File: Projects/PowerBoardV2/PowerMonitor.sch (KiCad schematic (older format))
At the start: 33 parts, among them M1 Teensy3, P19 CAN_CONN, P20 BAT_CONN, U1 ACS712, U2 MCP2562, U3 ACS712

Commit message: Trying to replace current resistors with surface mount resistors
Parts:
- R1, R10, R11, R12, R13, R14, R15, R16, R17, R18, R19, R2, R20, R3, R4, R5, R6, R7, R8, R9: footprint Resistors_ThroughHole:Resistor_Horizontal_RM7mm -> Resistors_SMD:R_0805_HandSoldering
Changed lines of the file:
@@
 F 0 "R1" V 4030 3300 50  0000 C CNN
 F 1 "2k" V 3950 3300 50  0000 C CNN
-F 2 "Resistors_ThroughHole:Resistor_Horizontal_RM7mm" V 3880 3300 50  0001 C CNN
+F 2 "Resistors_SMD:R_0805_HandSoldering" V 3880 3300 50  0001 C CNN
 F 3 "" H 3950 3300 50  0000 C CNN
 	1    3950 3300
@@
 F 0 "R2" V 4280 3500 50  0000 C CNN
 F 1 "10k" V 4200 3500 50  0000 C CNN
-F 2 "Resistors_ThroughHole:Resistor_Horizontal_RM7mm" V 4130 3500 50  0001 C CNN
+F 2 "Resistors_SMD:R_0805_HandSoldering" V 4130 3500 50  0001 C CNN
 F 3 "" H 4200 3500 50  0000 C CNN
 	1    4200 3500
@@
 F 0 "R5" V 6980 3650 50  0000 C CNN
 F 1 "886k" V 6900 3650 50  0000 C CNN
-F 2 "Resistors_ThroughHole:Resistor_Horizontal_RM7mm" V 6830 3650 50  0001 C CNN
+F 2 "Resistors_SMD:R_0805_HandSoldering" V 6830 3650 50  0001 C CNN
 F 3 "" H 6900 3650 50  0000 C CNN
 	1    6900 3650
@@
 F 0 "R6" V 6980 3850 50  0000 C CNN
 F 1 "870k" V 6900 3850 50  0000 C CNN
-F 2 "Resistors_ThroughHole:Resistor_Horizontal_RM7mm" V 6830 3850 50  0001 C CNN
+F 2 "Resistors_SMD:R_0805_HandSoldering" V 6830 3850 50  0001 C CNN
 F 3 "" H 6900 3850 50  0000 C CNN
 	1    6900 3850
@@
 F 0 "R7" V 6980 4050 50  0000 C CNN
 F 1 "848k" V 6900 4050 50  0000 C CNN
-F 2 "Resistors_ThroughHole:Resistor_Horizontal_RM7mm" V 6830 4050 50  0001 C CNN
+F 2 "Resistors_SMD:R_0805_HandSoldering" V 6830 4050 50  0001 C CNN
 F 3 "" H 6900 4050 50  0000 C CNN
 	1    6900 4050
@@
 F 0 "R8" V 6980 4250 50  0000 C CNN
 F 1 "818k" V 6900 4250 50  0000 C CNN
-F 2 "Resistors_ThroughHole:Resistor_Horizontal_RM7mm" V 6830 4250 50  0001 C CNN
+F 2 "Resistors_SMD:R_0805_HandSoldering" V 6830 4250 50  0001 C CNN
 F 3 "" H 6900 4250 50  0000 C CNN
 	1    6900 4250
@@
 F 0 "R9" V 6980 4450 50  0000 C CNN
 F 1 "773k" V 6900 4450 50  0000 C CNN
-F 2 "Resistors_ThroughHole:Resistor_Horizontal_RM7mm" V 6830 4450 50  0001 C CNN
+F 2 "Resistors_SMD:R_0805_HandSoldering" V 6830 4450 50  0001 C CNN
 F 3 "" H 6900 4450 50  0000 C CNN
 	1    6900 4450
@@
 F 0 "R10" V 6980 4650 50  0000 C CNN
 F 1 "697k" V 6900 4650 50  0000 C CNN
-F 2 "Resistors_ThroughHole:Resistor_Horizontal_RM7mm" V 6830 4650 50  0001 C CNN
+F 2 "Resistors_SMD:R_0805_HandSoldering" V 6830 4650 50  0001 C CNN
 F 3 "" H 6900 4650 50  0000 C CNN
 	1    6900 4650
@@
 F 0 "R11" V 6980 4850 50  0000 C CNN
 F 1 "545k" V 6900 4850 50  0000 C CNN
-F 2 "Resistors_ThroughHole:Resistor_Horizontal_RM7mm" V 6830 4850 50  0001 C CNN
+F 2 "Resistors_SMD:R_0805_HandSoldering" V 6830 4850 50  0001 C CNN
 F 3 "" H 6900 4850 50  0000 C CNN
 	1    6900 4850
@@
 F 0 "R12" V 6980 5050 50  0000 C CNN
 F 1 "90.9k" V 6900 5050 50  0000 C CNN
-F 2 "Resistors_ThroughHole:Resistor_Horizontal_RM7mm" V 6830 5050 50  0001 C CNN
+F 2 "Resistors_SMD:R_0805_HandSoldering" V 6830 5050 50  0001 C CNN
 F 3 "" H 6900 5050 50  0000 C CNN
 	1    6900 5050
@@
 F 0 "R13" V 7280 5250 50  0000 C CNN
 F 1 "909k" V 7200 5250 50  0000 C CNN
-F 2 "Resistors_ThroughHole:Resistor_Horizontal_RM7mm" V 7130 5250 50  0001 C CNN
+F 2 "Resistors_SMD:R_0805_HandSoldering" V 7130 5250 50  0001 C CNN
 F 3 "" H 7200 5250 50  0000 C CNN
 	1    7200 5250
@@
 F 0 "R14" V 7480 5250 50  0000 C CNN
 F 1 "455k" V 7400 5250 50  0000 C CNN
-F 2 "Resistors_ThroughHole:Resistor_Horizontal_RM7mm" V 7330 5250 50  0001 C CNN
+F 2 "Resistors_SMD:R_0805_HandSoldering" V 7330 5250 50  0001 C CNN
 F 3 "" H 7400 5250 50  0000 C CNN
 	1    7400 5250
@@
 F 0 "R15" V 7680 5250 50  0000 C CNN
 F 1 "303k" V 7600 5250 50  0000 C CNN
-F 2 "Resistors_ThroughHole:Resistor_Horizontal_RM7mm" V 7530 5250 50  0001 C CNN
+F 2 "Resistors_SMD:R_0805_HandSoldering" V 7530 5250 50  0001 C CNN
 F 3 "" H 7600 5250 50  0000 C CNN
 	1    7600 5250
@@
 F 0 "R16" V 7880 5250 50  0000 C CNN
 F 1 "227k" V 7800 5250 50  0000 C CNN
-F 2 "Resistors_ThroughHole:Resistor_Horizontal_RM7mm" V 7730 5250 50  0001 C CNN
+F 2 "Resistors_SMD:R_0805_HandSoldering" V 7730 5250 50  0001 C CNN
 F 3 "" H 7800 5250 50  0000 C CNN
 	1    7800 5250
@@
 F 0 "R17" V 8080 5250 50  0000 C CNN
 F 1 "182k" V 8000 5250 50  0000 C CNN
-F 2 "Resistors_ThroughHole:Resistor_Horizontal_RM7mm" V 7930 5250 50  0001 C CNN
+F 2 "Resistors_SMD:R_0805_HandSoldering" V 7930 5250 50  0001 C CNN
 F 3 "" H 8000 5250 50  0000 C CNN
 	1    8000 5250
@@
 F 0 "R18" V 8280 5250 50  0000 C CNN
 F 1 "152k" V 8200 5250 50  0000 C CNN
-F 2 "Resistors_ThroughHole:Resistor_Horizontal_RM7mm" V 8130 5250 50  0001 C CNN
+F 2 "Resistors_SMD:R_0805_HandSoldering" V 8130 5250 50  0001 C CNN
 F 3 "" H 8200 5250 50  0000 C CNN
 	1    8200 5250
@@
 F 0 "R19" V 8480 5250 50  0000 C CNN
 F 1 "130k" V 8400 5250 50  0000 C CNN
-F 2 "Resistors_ThroughHole:Resistor_Horizontal_RM7mm" V 8330 5250 50  0001 C CNN
+F 2 "Resistors_SMD:R_0805_HandSoldering" V 8330 5250 50  0001 C CNN
 F 3 "" H 8400 5250 50  0000 C CNN
 	1    8400 5250
@@
 F 0 "R20" V 8680 5250 50  0000 C CNN
 F 1 "114k" V 8600 5250 50  0000 C CNN
-F 2 "Resistors_ThroughHole:Resistor_Horizontal_RM7mm" V 8530 5250 50  0001 C CNN
+F 2 "Resistors_SMD:R_0805_HandSoldering" V 8530 5250 50  0001 C CNN
 F 3 "" H 8600 5250 50  0000 C CNN
 	1    8600 5250
@@
 F 0 "R3" V 3980 4450 50  0000 C CNN
 F 1 "2k" V 3900 4450 50  0000 C CNN
-F 2 "Resistors_ThroughHole:Resistor_Horizontal_RM7mm" V 3830 4450 50  0001 C CNN
+F 2 "Resistors_SMD:R_0805_HandSoldering" V 3830 4450 50  0001 C CNN
 F 3 "" H 3900 4450 50  0000 C CNN
 	1    3900 4450
@@
 F 0 "R4" V 4230 4650 50  0000 C CNN
 F 1 "10k" V 4150 4650 50  0000 C CNN
-F 2 "Resistors_ThroughHole:Resistor_Horizontal_RM7mm" V 4080 4650 50  0001 C CNN
+F 2 "Resistors_SMD:R_0805_HandSoldering" V 4080 4650 50  0001 C CNN
 F 3 "" H 4150 4650 50  0000 C CNN
 	1    4150 4650

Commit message: Updated Power Distribution Board and refs
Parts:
- C1, C2, C3, C4, C5: footprint Capacitors_ThroughHole:C_Radial_D5_L6_P2.5 -> Capacitors_SMD:C_1210
- D1, D2: footprint Diodes_ThroughHole:Diode_DO-35_SOD27_Horizontal_RM10 -> Diodes_SMD:D_SOD-123
- M1: footprint USSTPARTS:TEENSY3.2 -> USST-footprints:Teensy_3.2_NoTail
- P19: footprint Pin_Headers:Pin_Header_Straight_1x04 -> USST-footprints:Molex_39502_1004R
- P20: footprint Pin_Headers:Pin_Header_Straight_1x09 -> USST-footprints:Molex_39502_1009R
- U2: footprint Housings_DIP:DIP-8_W7.62mm -> Housings_SOIC:SOIC-8_3.9x4.9mm_Pitch1.27mm
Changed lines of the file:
@@
 LIBS:contrib
 LIBS:valves
+LIBS:USST-parts
 LIBS:PowerBoardV2-cache
 EELAYER 25 0
@@
 F 0 "C1" H 3910 3570 50  0000 L CNN
 F 1 "1nF" H 3910 3420 50  0000 L CNN
-F 2 "Capacitors_ThroughHole:C_Radial_D5_L6_P2.5" H 3900 3500 50  0001 C CNN
+F 2 "Capacitors_SMD:C_1210" H 3900 3500 50  0001 C CNN
 F 3 "" H 3900 3500 50  0000 C CNN
 	1    3900 3500
@@
 F 0 "D1" H 4400 3400 50  0000 C CNN
 F 1 "1N4448W" H 4400 3200 50  0000 C CNN
-F 2 "Diodes_ThroughHole:Diode_DO-35_SOD27_Horizontal_RM10" H 4400 3300 50  0001 C CNN
+F 2 "Diodes_SMD:D_SOD-123" H 4400 3300 50  0001 C CNN
 F 3 "" H 4400 3300 50  0000 C CNN
 	1    4400 3300
@@
 F 0 "U2" H 7050 2300 60  0000 C CNN
 F 1 "MCP2562" H 6850 1700 60  0000 C CNN
-F 2 "Housings_DIP:DIP-8_W7.62mm" H 6600 1900 60  0001 C CNN
+F 2 "Housings_SOIC:SOIC-8_3.9x4.9mm_Pitch1.27mm" H 6600 1900 60  0001 C CNN
 F 3 "" H 6600 1900 60  0000 C CNN
 	1    6850 2000
@@
 F 0 "C2" H 5910 2070 50  0000 L CNN
 F 1 "0.1uF" H 5910 1920 50  0000 L CNN
-F 2 "Capacitors_ThroughHole:C_Radial_D5_L6_P2.5" H 5900 2000 50  0001 C CNN
+F 2 "Capacitors_SMD:C_1210" H 5900 2000 50  0001 C CNN
 F 3 "" H 5900 2000 50  0000 C CNN
 	1    5900 2000
@@
 F 0 "C3" H 4610 3520 50  0000 L CNN
 F 1 "Test" H 4610 3370 50  0000 L CNN
-F 2 "Capacitors_ThroughHole:C_Radial_D5_L6_P2.5" H 4600 3450 50  0001 C CNN
+F 2 "Capacitors_SMD:C_1210" H 4600 3450 50  0001 C CNN
 F 3 "" H 4600 3450 50  0000 C CNN
 	1    4600 3450
@@
 F 0 "C4" H 3860 4720 50  0000 L CNN
 F 1 "1nF" H 3860 4570 50  0000 L CNN
-F 2 "Capacitors_ThroughHole:C_Radial_D5_L6_P2.5" H 3850 4650 50  0001 C CNN
+F 2 "Capacitors_SMD:C_1210" H 3850 4650 50  0001 C CNN
 F 3 "" H 3850 4650 50  0000 C CNN
 	1    3850 4650
@@
 F 0 "D2" H 4350 4550 50  0000 C CNN
 F 1 "1N4448W" H 4350 4350 50  0000 C CNN
-F 2 "Diodes_ThroughHole:Diode_DO-35_SOD27_Horizontal_RM10" H 4350 4450 50  0001 C CNN
+F 2 "Diodes_SMD:D_SOD-123" H 4350 4450 50  0001 C CNN
 F 3 "" H 4350 4450 50  0000 C CNN
 	1    4350 4450
@@
 F 0 "C5" H 4560 4670 50  0000 L CNN
 F 1 "Test" H 4560 4520 50  0000 L CNN
-F 2 "Capacitors_ThroughHole:C_Radial_D5_L6_P2.5" H 4550 4600 50  0001 C CNN
+F 2 "Capacitors_SMD:C_1210" H 4550 4600 50  0001 C CNN
 F 3 "" H 4550 4600 50  0000 C CNN
 	1    4550 4600
@@
 F 0 "P19" V 4150 2000 50  0000 C CNN
 F 1 "CAN_CONN" V 4250 2000 50  0000 C CNN
-F 2 "Pin_Headers:Pin_Header_Straight_1x04" H 4200 2000 60  0001 C CNN
+F 2 "USST-footprints:Molex_39502_1004R" H 4200 2000 60  0001 C CNN
 F 3 "" H 4200 2000 60  0000 C CNN
 	1    4200 2000
@@
 F 0 "P20" V 5600 4550 60  0000 C CNN
 F 1 "BAT_CONN" V 5700 4550 60  0000 C CNN
-F 2 "Pin_Headers:Pin_Header_Straight_1x09" H 5650 4550 60  0001 C CNN
+F 2 "USST-footprints:Molex_39502_1009R" H 5650 4550 60  0001 C CNN
 F 3 "" H 5650 4550 60  0000 C CNN
 	1    5650 4550
@@
 F 0 "M1" H 8300 2150 60  0000 C CNN
 F 1 "Teensy3" H 8700 2150 60  0000 C CNN
-F 2 "USSTPARTS:TEENSY3.2" H 8550 1700 60  0001 C CNN
+F 2 "USST-footprints:Teensy_3.2_NoTail" H 8550 1700 60  0001 C CNN
 F 3 "" H 8550 1700 60  0000 C CNN
 	1    8550 1700

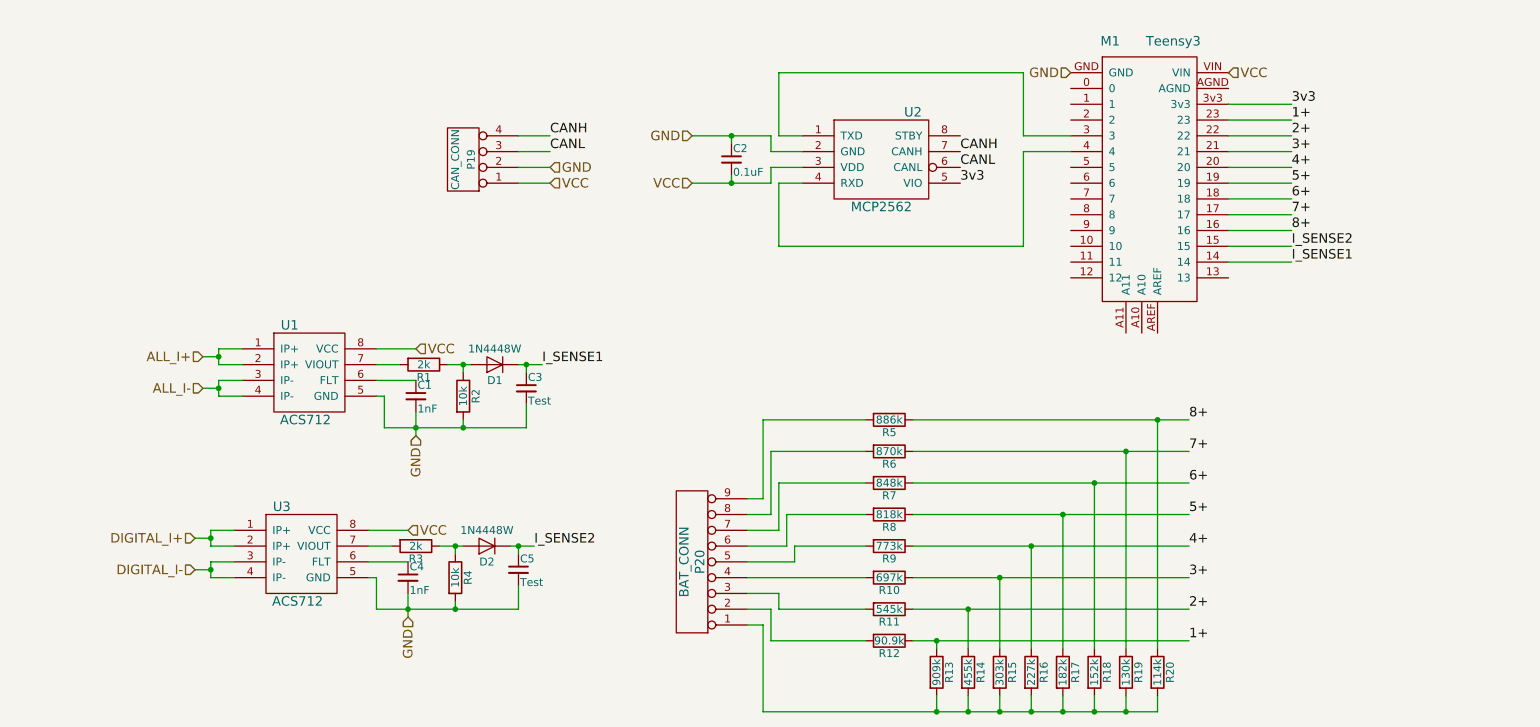
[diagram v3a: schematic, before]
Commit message: added notes for layout of the power board
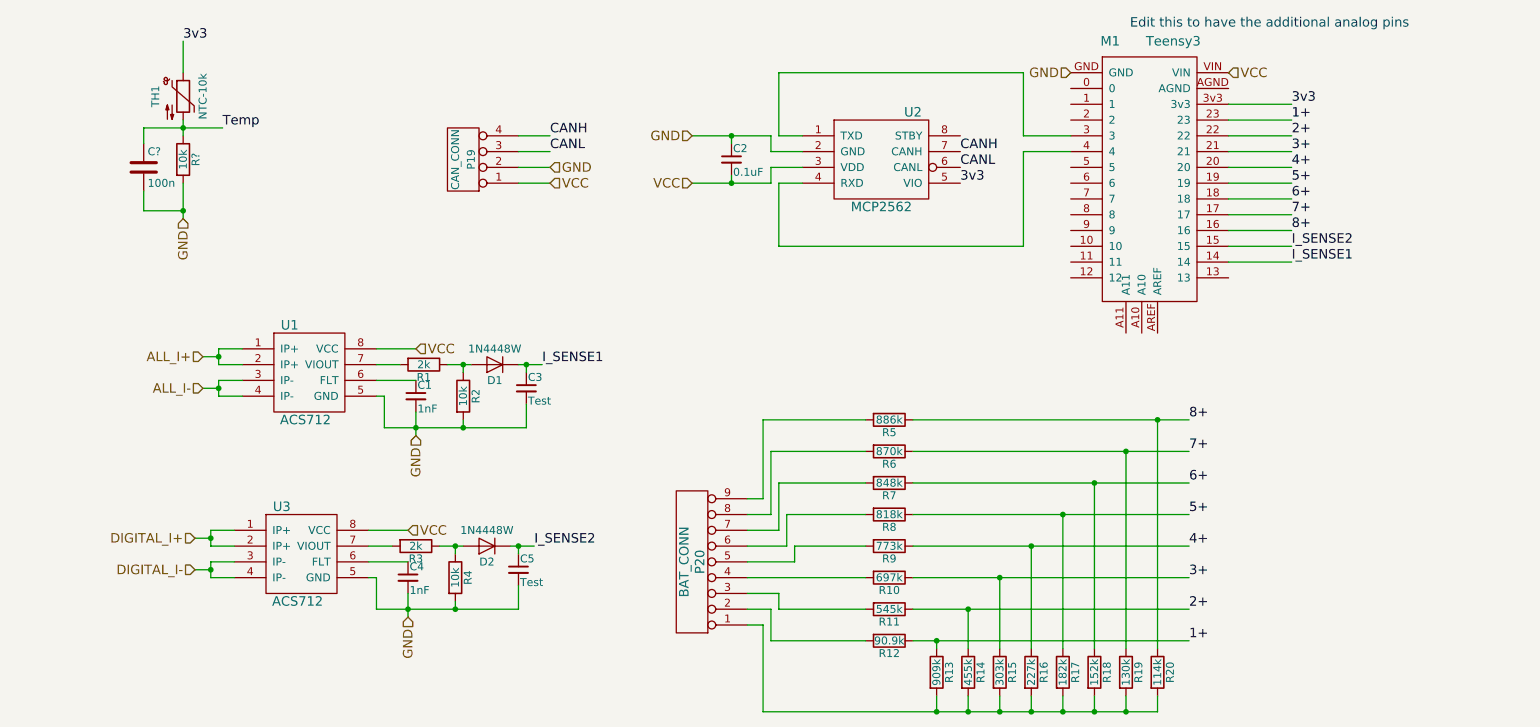
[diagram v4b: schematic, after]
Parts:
- added C?: 100n, symbol C
- added R?: 10k, symbol R
- added TH1: NTC-10k, symbol Thermistor_NTC
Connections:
- net 3v3: now also TH1.1
- net GND: now also C?.2, R?.2
- new net Temp: C?.1, R?.1, TH1.2
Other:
- note added: "Edit this to have the additional analog pins\n"
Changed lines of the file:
@@
 	1    0    0    -1
 $EndComp
+$Comp
+L Thermistor_NTC TH1
+U 1 1 589F7A12
+P 2425 1600
+F 0 "TH1" V 2250 1600 50  0000 C CNN
+F 1 "NTC-10k" V 2550 1600 50  0000 C CNN
+F 2 "" H 2425 1650 50  0001 C CNN
+F 3 "" H 2425 1650 50  0001 C CNN
+	1    2425 1600
+	1    0    0    -1
+$EndComp
+$Comp
+L R R?
+U 1 1 589F84C3
+P 2425 2000
+F 0 "R?" V 2505 2000 50  0000 C CNN
+F 1 "10k" V 2425 2000 50  0000 C CNN
+F 2 "" V 2355 2000 50  0000 C CNN
+F 3 "" H 2425 2000 50  0000 C CNN
+	1    2425 2000
+	1    0    0    -1
+$EndComp
+Wire Wire Line
+	2425 1750 2425 1850
+Wire Wire Line
+	2425 1450 2425 1250
+Wire Wire Line
+	2425 2150 2425 2375
+Text Label 2425 1250 0    60   ~ 0
+3v3
+Text HLabel 2425 2375 3    60   Input ~ 0
+GND
+Wire Wire Line
+	2175 1800 2675 1800
+Wire Wire Line
+	2175 1800 2175 1900
+Connection ~ 2425 1800
+Wire Wire Line
+	2175 2325 2425 2325
+Wire Wire Line
+	2175 2200 2175 2325
+Connection ~ 2425 2325
+$Comp
+L C C?
+U 1 1 589FA449
+P 2175 2050
+F 0 "C?" H 2200 2150 50  0000 L CNN
+F 1 "100n" H 2200 1950 50  0000 L CNN
+F 2 "" H 2213 1900 50  0000 C CNN
+F 3 "" H 2175 2050 50  0000 C CNN
+	1    2175 2050
+	1    0    0    -1
+$EndComp
+Text Label 2675 1800 0    60   ~ 0
+Temp
+Text Notes 8425 1175 0    60   ~ 0
+Edit this to have the additional analog pins\n
 $EndSCHEMATC

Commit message: Almost done just need to add silk screen stuff
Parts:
- C6: renamed from C?; footprint (none) -> Capacitors_SMD:C_0805_HandSoldering
- R21: renamed from R?; footprint (none) -> Resistors_SMD:R_0805_HandSoldering
- TH1: footprint (none) -> Resistors_SMD:R_0805_HandSoldering
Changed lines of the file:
@@
 F 0 "TH1" V 2250 1600 50  0000 C CNN
 F 1 "NTC-10k" V 2550 1600 50  0000 C CNN
-F 2 "" H 2425 1650 50  0001 C CNN
+F 2 "Resistors_SMD:R_0805_HandSoldering" H 2425 1650 50  0001 C CNN
 F 3 "" H 2425 1650 50  0001 C CNN
 	1    2425 1600
@@
 $EndComp
 $Comp
-L R R?
+L R R21
 U 1 1 589F84C3
 P 2425 2000
-F 0 "R?" V 2505 2000 50  0000 C CNN
+F 0 "R21" V 2505 2000 50  0000 C CNN
 F 1 "10k" V 2425 2000 50  0000 C CNN
-F 2 "" V 2355 2000 50  0000 C CNN
+F 2 "Resistors_SMD:R_0805_HandSoldering" V 2355 2000 50  0000 C CNN
 F 3 "" H 2425 2000 50  0000 C CNN
 	1    2425 2000
@@
 Connection ~ 2425 2325
 $Comp
-L C C?
+L C C6
 U 1 1 589FA449
 P 2175 2050
-F 0 "C?" H 2200 2150 50  0000 L CNN
+F 0 "C6" H 2200 2150 50  0000 L CNN
 F 1 "100n" H 2200 1950 50  0000 L CNN
-F 2 "" H 2213 1900 50  0000 C CNN
+F 2 "Capacitors_SMD:C_0805_HandSoldering" H 2213 1900 50  0000 C CNN
 F 3 "" H 2175 2050 50  0000 C CNN
 	1    2175 2050

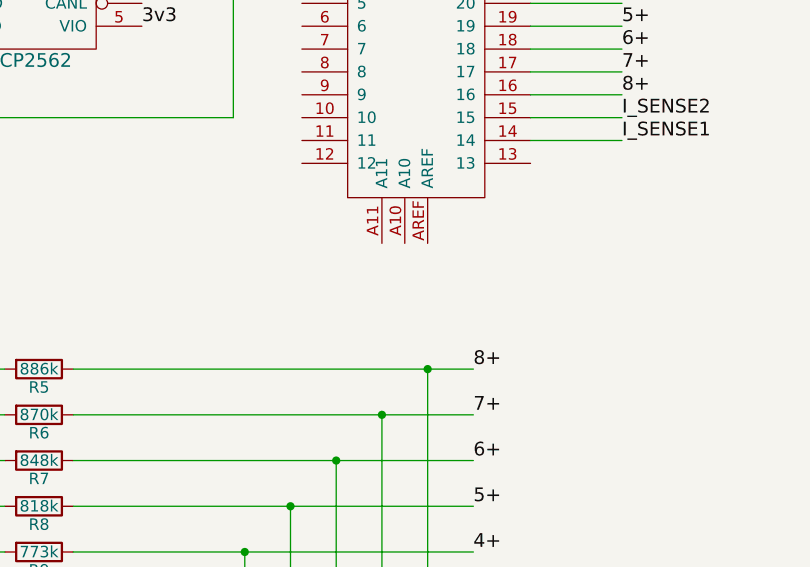
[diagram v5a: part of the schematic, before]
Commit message: edited VESC Card Breakout, redid footprint
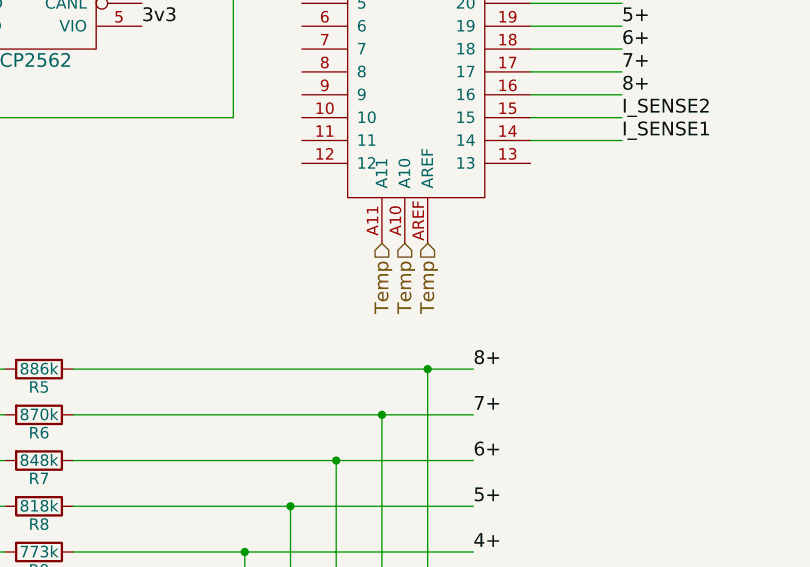
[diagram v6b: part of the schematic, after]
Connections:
- net Temp: now also M1.A10, M1.A11, M1.AREF
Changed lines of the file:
@@
 Text Notes 8425 1175 0    60   ~ 0
 Edit this to have the additional analog pins\n
+Text HLabel 8400 3100 3    60   Input ~ 0
+Temp
+Text HLabel 8500 3100 3    60   Input ~ 0
+Temp
+Text HLabel 8600 3100 3    60   Input ~ 0
+Temp
 $EndSCHEMATC

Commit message: added BOM for backplane
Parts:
- M1: symbol Teensy3 -> Teensy3-RESCUE-PowerBoardV2
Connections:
- net Temp: no longer M1.A10, M1.AREF
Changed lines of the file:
@@
 EESchema Schematic File Version 2
+LIBS:PowerBoardV2-rescue
 LIBS:power
 LIBS:device
@@
 	6300 4550 6300 4450
 $Comp
-L Teensy3 M1
+L Teensy3-RESCUE-PowerBoardV2 M1
 U 1 1 56F8FB22
 P 8550 1700
+AR Path="/56F8FB22" Ref="M1"  Part="1"
+AR Path="/56F72A99/56F8FB22" Ref="M1"  Part="1"
 F 0 "M1" H 8300 2150 60  0000 C CNN
 F 1 "Teensy3" H 8700 2150 60  0000 C CNN
@@
 Text Notes 8425 1175 0    60   ~ 0
 Edit this to have the additional analog pins\n
-Text HLabel 8400 3100 3    60   Input ~ 0
-Temp
-Text HLabel 8500 3100 3    60   Input ~ 0
-Temp
-Text HLabel 8600 3100 3    60   Input ~ 0
+Text Label 8400 3100 3    60   ~ 0
 Temp
 $EndSCHEMATC
